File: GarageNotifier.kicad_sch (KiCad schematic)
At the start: 77 parts, among them J1 NF-U.FL, J2 FTSH-105-01-F-DV-K, J3 Conn_01x05, SW1 PTS647SK50SMTR2LFS, SW2 NF-Reed NO, U1 MDBT42Q-512KV2, U2 RFM95W-868S2, U3 SM351LT, U4 LIS3DH, Y1 32.768kHz

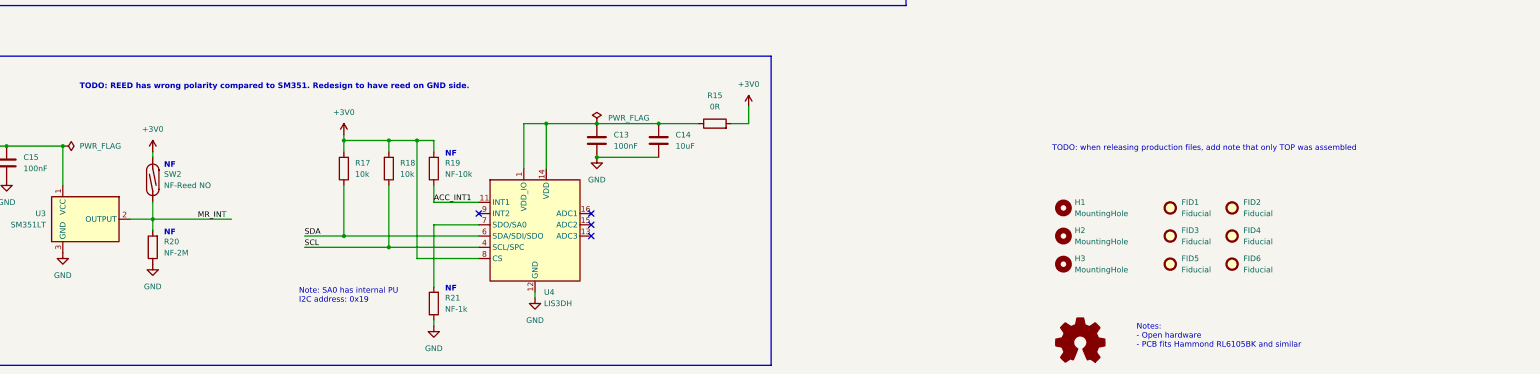
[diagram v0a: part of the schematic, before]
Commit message: Added release files
Added zip files with PCB production and assembling info used for JLCPCB. Removed digikey project library (now it is kicad global).
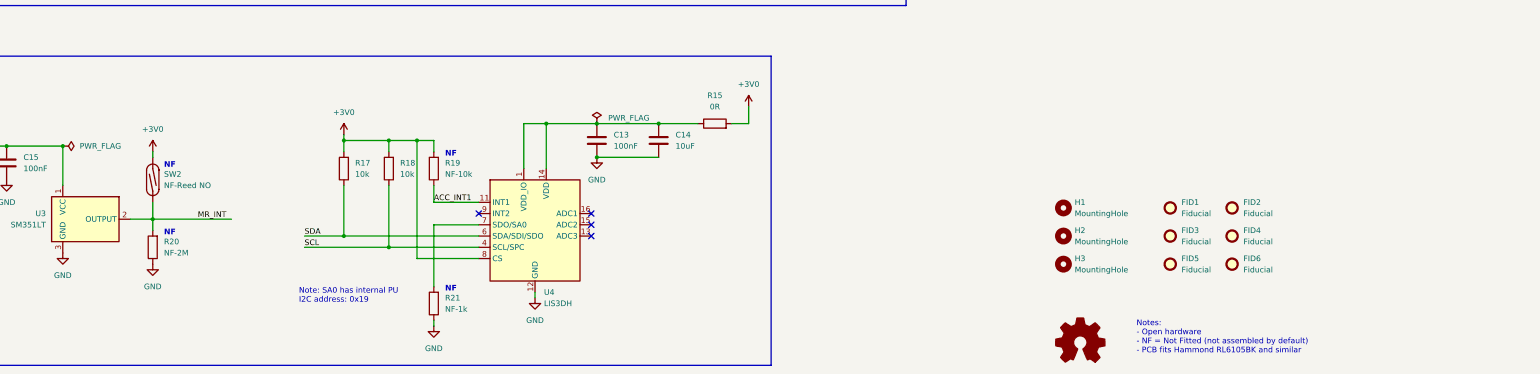
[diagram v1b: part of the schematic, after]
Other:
- note added: "Notes: - Open hardware - NF = Not Fitted (not assembled by default) - PCB fits Hammond RL6105BK and similar"
- note removed: "Notes: - Open hardware - PCB fits Hammond RL6105BK and similar"
- note removed: "TODO: REED has wrong polarity compared to SM351. Redesign to have reed on GND side."
- note removed: "TODO: when releasing production files, add note that only TOP was assembled"
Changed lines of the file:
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@@
   (title_block
     (title "GarageNotifier")
-    (date "2022-04-02")
+    (date "2022-08-15")
     (rev "v1.0.0")
     (comment 1 "Drawn by: Zvonko Bockaj")
